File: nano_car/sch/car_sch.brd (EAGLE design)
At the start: 23 x 22 mm, 24 parts, among them M1+ PTR1TP11R, M1- PTR1TP11R, M2+ PTR1TP11R, M2- PTR1TP11R, U1 ATTINY10-TSHR, U2 TSOP382

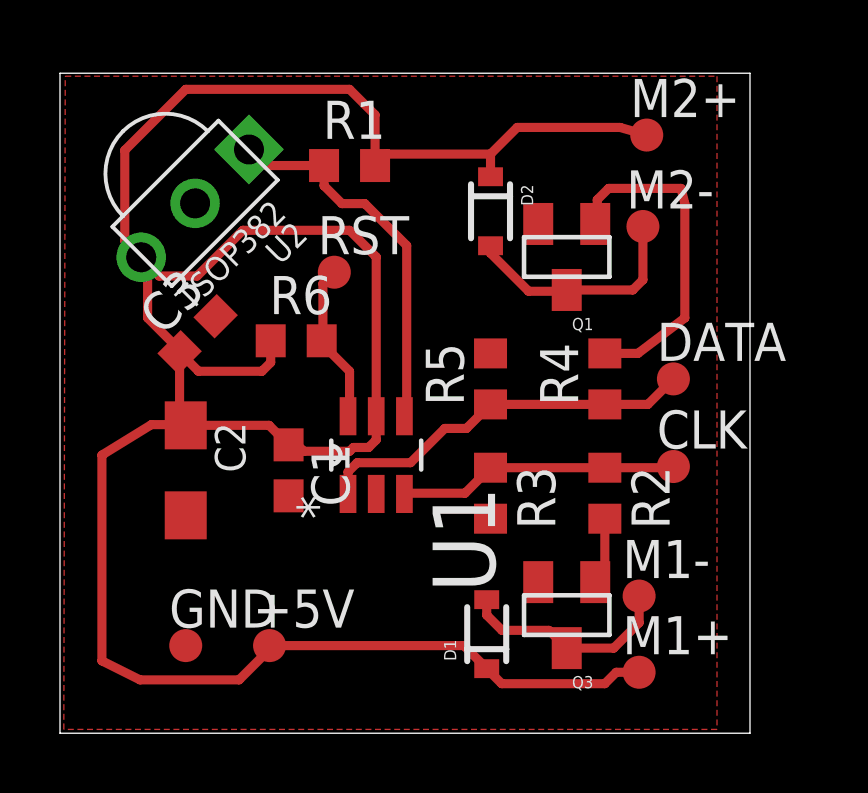
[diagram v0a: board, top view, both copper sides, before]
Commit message: Fix wire spacing
More spacing between wire for freely laser-iron production
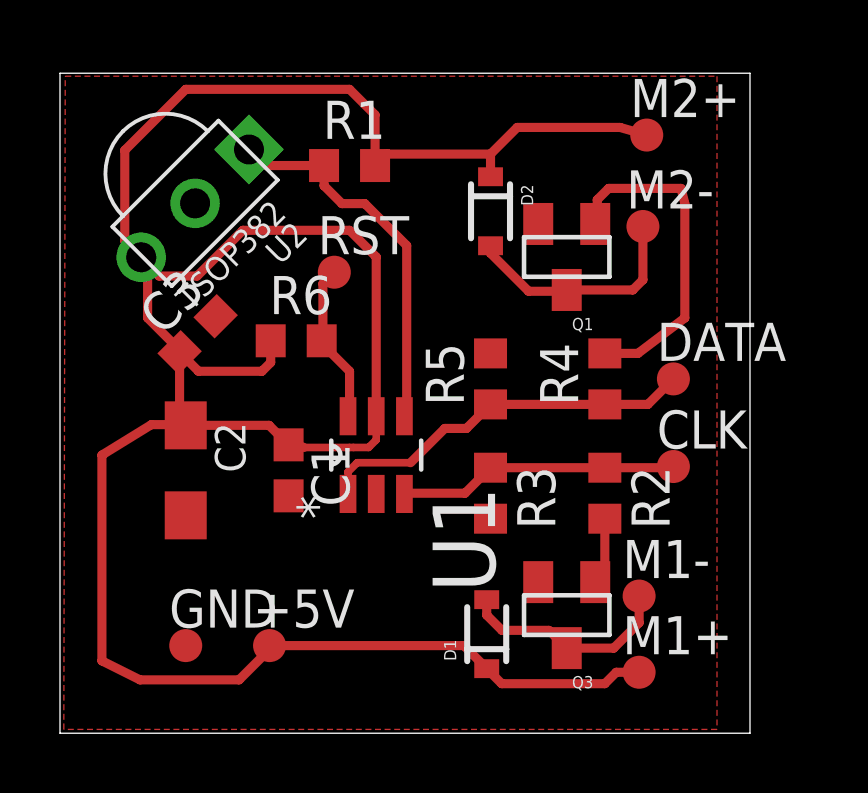
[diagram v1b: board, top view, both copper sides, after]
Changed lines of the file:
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@@
 <contactref element="Q1" pad="2"/>
 <contactref element="R5" pad="2"/>
-<polygon width="0.1" layer="1">
+<polygon width="0.1" layer="1" isolate="0.254">
 <vertex x="0.175" y="21.9"/>
 <vertex x="21.9" y="21.9"/>
@@
 <wire x1="4.064" y1="10.287" x2="4.191" y2="10.16" width="0.3048" layer="1"/>
 <wire x1="7.62" y1="9.613" x2="7.913" y2="9.613" width="0.3048" layer="1"/>
-<wire x1="7.913" y1="9.613" x2="8.128" y2="9.398" width="0.3048" layer="1"/>
-<wire x1="8.128" y1="9.398" x2="9.652" y2="9.398" width="0.3048" layer="1"/>
-<wire x1="9.652" y1="9.398" x2="9.779" y2="9.525" width="0.3048" layer="1"/>
-<wire x1="9.779" y1="9.525" x2="10.287" y2="9.525" width="0.3048" layer="1"/>
-<wire x1="10.287" y1="9.525" x2="10.541" y2="9.779" width="0.3048" layer="1"/>
-<wire x1="10.541" y1="9.779" x2="10.541" y2="10.5664" width="0.3048" layer="1"/>
+<wire x1="7.913" y1="9.613" x2="8.128" y2="9.525" width="0.3048" layer="1"/>
+<wire x1="8.128" y1="9.525" x2="9.652" y2="9.525" width="0.254" layer="1"/>
+<wire x1="9.652" y1="9.525" x2="9.779" y2="9.525" width="0.254" layer="1"/>
+<wire x1="9.779" y1="9.525" x2="10.287" y2="9.525" width="0.254" layer="1"/>
+<wire x1="10.287" y1="9.525" x2="10.541" y2="9.779" width="0.254" layer="1"/>
+<wire x1="10.541" y1="9.779" x2="10.541" y2="10.5664" width="0.254" layer="1"/>
 <wire x1="6.985" y1="2.921" x2="13.462" y2="2.921" width="0.3048" layer="1"/>
 <wire x1="13.462" y1="2.921" x2="14.224" y2="2.159" width="0.3048" layer="1"/>
@@
 <wire x1="13.55" y1="10.16" x2="12.827" y2="10.16" width="0.3048" layer="1"/>
 <wire x1="12.827" y1="10.16" x2="11.684" y2="9.017" width="0.3048" layer="1"/>
-<wire x1="11.684" y1="9.017" x2="9.906" y2="9.017" width="0.3048" layer="1"/>
-<wire x1="9.906" y1="9.017" x2="9.6012" y2="8.7122" width="0.3048" layer="1"/>
-<wire x1="9.6012" y1="8.7122" x2="9.6012" y2="7.9756" width="0.3048" layer="1"/>
+<wire x1="11.684" y1="9.017" x2="9.906" y2="9.017" width="0.254" layer="1"/>
+<wire x1="9.906" y1="9.017" x2="9.6012" y2="8.7122" width="0.254" layer="1"/>
+<wire x1="9.6012" y1="8.7122" x2="9.6012" y2="7.9756" width="0.254" layer="1"/>
 <wire x1="14.351" y1="10.961" x2="18.161" y2="10.961" width="0.3048" layer="1"/>
 <wire x1="20.447" y1="11.811" x2="19.597" y2="10.961" width="0.3048" layer="1"/>
